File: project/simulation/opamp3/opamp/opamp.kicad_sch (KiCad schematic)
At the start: 10 parts, among them U1 OPAMP, U2 OPAMP

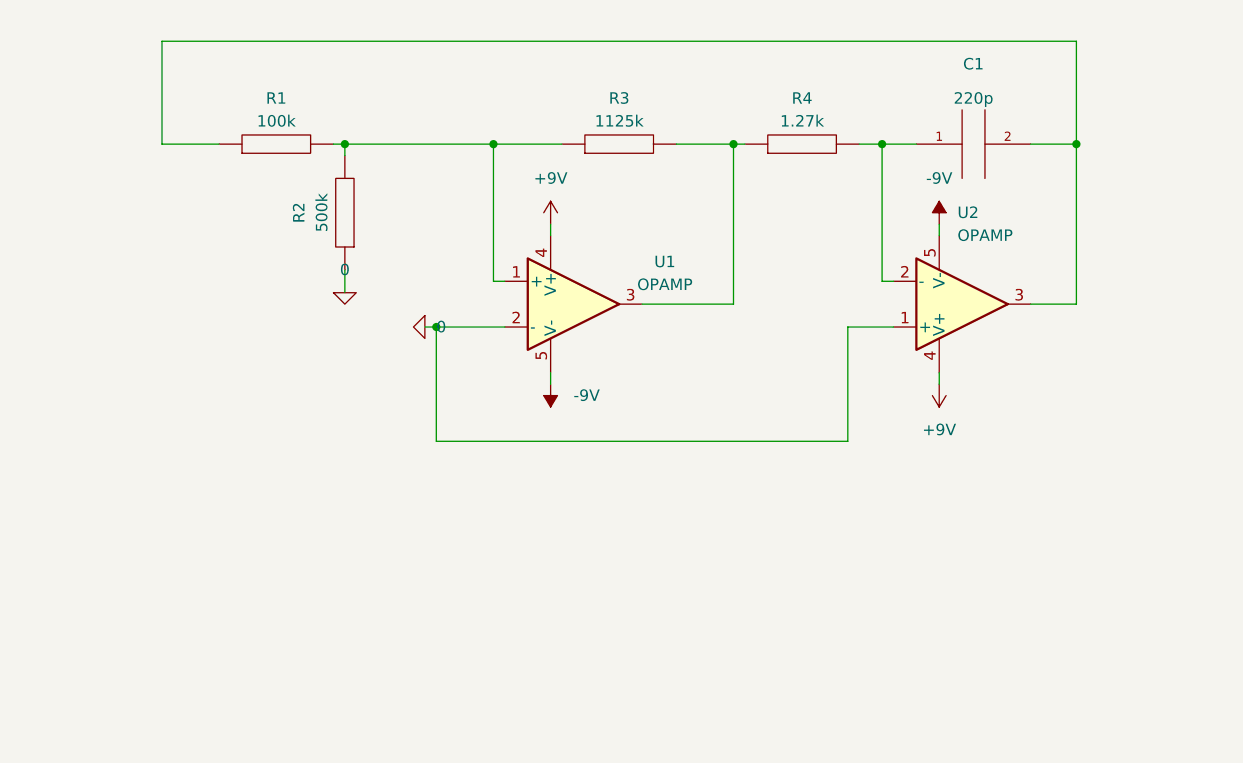
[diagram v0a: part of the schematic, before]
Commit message: I simulated different opamp circuits, I'm facing with problems on peaks when I increase frequency, I think I should change opamp's spice mode, if I overcome the issue, then I'll start to simulate transistor TWG
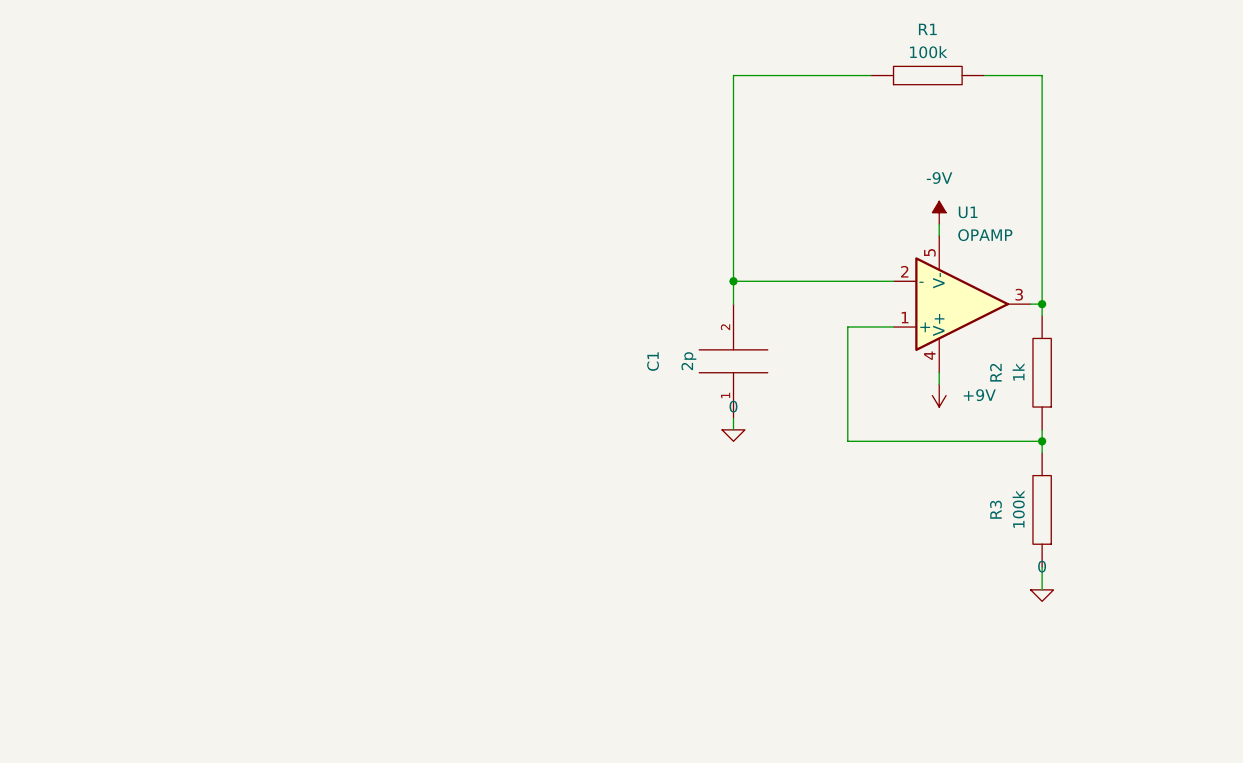
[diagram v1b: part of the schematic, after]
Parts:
- removed R4: 1, symbol pspice:R
- removed U2: OPAMP, symbol pspice:OPAMP
- C1: Spice_Model 220p -> 2p
- R2: Spice_Model 500k -> 1k
- R3: Spice_Model 1125k -> 100k
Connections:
- net 0: now also C1.1, R3.1; no longer R2.1, U1.2 (-)
- net at R1.2, R2.2: now also U1.3; no longer R3.1, U1.1 (+)
- net at R3.2: now also R2.1, U1.1 (+); no longer U1.3
- net at C1.2, R1.1: now also U1.2 (-)
